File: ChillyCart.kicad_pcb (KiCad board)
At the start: 2 copper layers, 51 x 60.7 mm, 14 parts, among them J1 GameBoy_GamePak_DMG-09, J2 USB_C_Receptacle_USB2.0_16P, U1 TXB0108PW, U2 TXB0108PW, U3 TXB0108PW, U4 RP2350_80QFN

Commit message: Added psram,flash,rtc,sd
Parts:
- added BT1: Battery_Cell, Battery:BatteryHolder_Keystone_103_1x20mm, F.Cu at (150.0, 63.8)
- added C10: 15p, Capacitor_SMD:C_0402_1005Metric, F.Cu at (128.7, 99.0)
- added C11: 100n, Capacitor_SMD:C_0402_1005Metric, F.Cu at (128.7, 101.0)
- added C12: DNF, Capacitor_SMD:C_0402_1005Metric, F.Cu at (166.5, 82.0)
- added C13: 100n, Capacitor_SMD:C_0402_1005Metric, F.Cu at (166.5, 84.0)
- added C14: 100n, Capacitor_SMD:C_0402_1005Metric, F.Cu at (138.1, 94.0)
- added C15: 100n, Capacitor_SMD:C_0402_1005Metric, F.Cu at (131.6, 97.0)
- added C16: 100n, Capacitor_SMD:C_0402_1005Metric, F.Cu at (131.6, 99.0)
- added C17: 100n, Capacitor_SMD:C_0402_1005Metric, F.Cu at (131.6, 101.0)
- added C18: 100n, Capacitor_SMD:C_0402_1005Metric, F.Cu at (169.3, 82.0)
- added C19: 100n, Capacitor_SMD:C_0402_1005Metric, F.Cu at (169.3, 84.0)
- added C20: 100n, Capacitor_SMD:C_0402_1005Metric, F.Cu at (140.9, 94.0)
- added C21: 100n, Capacitor_SMD:C_0402_1005Metric, F.Cu at (134.5, 97.0)
- added C24: 4.7u, Capacitor_SMD:C_0402_1005Metric, F.Cu at (134.5, 99.0)
- added C25: 100n, Capacitor_SMD:C_0402_1005Metric, F.Cu at (134.5, 101.0)
- added C26: 4.7u, Capacitor_SMD:C_0402_1005Metric, F.Cu at (172.2, 82.0)
- added C27: 100n, Capacitor_SMD:C_0402_1005Metric, F.Cu at (172.2, 84.0)
- added C28: 10u, Capacitor_SMD:C_0805_2012Metric, F.Cu at (162.9, 100.5)
- added C7: 10u, Capacitor_SMD:C_0805_2012Metric, F.Cu at (158.9, 100.5)
- added C7: 100nF, Capacitor_SMD:C_0603_1608Metric_Pad1.08x0.95mm_HandSolder, F.Cu at (138.7, 89.2)
- added C8: 100nF, Capacitor_SMD:C_0603_1608Metric_Pad1.08x0.95mm_HandSolder, F.Cu at (138.7, 91.7)
- added C9: 15p, Capacitor_SMD:C_0402_1005Metric, F.Cu at (128.7, 97.0)
- added J3: Micro_SD_Card_Det1, kicad-open-modules:TF-015, F.Cu at (135.5, 83.3)
- added R10: 27, Resistor_SMD:R_0402_1005Metric, F.Cu at (164.2, 82.0)
- added R11: 27, Resistor_SMD:R_0402_1005Metric, F.Cu at (164.2, 84.0)
- added R3: 1k, Resistor_SMD:R_0402_1005Metric, F.Cu at (138.1, 96.0)
- added R4: DNF, Resistor_SMD:R_0402_1005Metric, F.Cu at (158.4, 82.0)
- added R5: 0, Resistor_SMD:R_0402_1005Metric, F.Cu at (158.4, 84.0)
- added R6: DNF, Resistor_SMD:R_0402_1005Metric, F.Cu at (141.0, 96.0)
- added R7: DNF, Resistor_SMD:R_0402_1005Metric, F.Cu at (161.3, 82.0)
- added R8: DNF, Resistor_SMD:R_0402_1005Metric, F.Cu at (161.3, 84.0)
- added R9: 33, Resistor_SMD:R_0402_1005Metric, F.Cu at (143.9, 96.0)
- added U5: AMS1117-3.3, Package_TO_SOT_SMD:SOT-223-3_TabPin2, F.Cu at (131.6, 92.2)
- added U6: W25Q128JVS, Package_SO:SOIC-8_5.23x5.23mm_P1.27mm, F.Cu at (150.5, 96.0)
- added U7: DNF, Package_SO:SOIC-8_5.23x5.23mm_P1.27mm, F.Cu at (150.4, 104.9)
- added U8: MCP7940N-xMNY, Package_DFN_QFN:DFN-8-1EP_3x2mm_P0.5mm_EP1.36x1.46mm, F.Cu at (141.0, 99.8)
- added Y1: ABM8-272-T3, Crystal:Crystal_SMD_3225-4Pin_3.2x2.5mm, F.Cu at (168.0, 100.5)
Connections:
- U4 pad 10: unconnected-(U4-DVDD-Pad10) -> +1V1
- U4 pad 15: unconnected-(U4-IOVDD-Pad15) -> +3V3
- U4 pad 24: unconnected-(U4-IOVDD-Pad24) -> +3V3
- U4 pad 29: unconnected-(U4-IOVDD-Pad29) -> +3V3
- U4 pad 32: unconnected-(U4-DVDD-Pad32) -> +1V1
- U4 pad 41: unconnected-(U4-IOVDD-Pad41) -> +3V3
- U4 pad 5: unconnected-(U4-IOVDD-Pad5) -> +3V3
- U4 pad 50: unconnected-(U4-IOVDD-Pad50) -> +3V3
- U4 pad 51: unconnected-(U4-DVDD-Pad51) -> +1V1
- U4 pad 59: unconnected-(U4-ADC_AVDD-Pad59) -> +3V3
- U4 pad 60: unconnected-(U4-IOVDD-Pad60) -> +3V3
- U4 pad 61: unconnected-(U4-VREG_AVDD-Pad61) -> /VREG_AVDD
- U4 pad 62: unconnected-(U4-VREG_PGND-Pad62) -> GND
- U4 pad 63: unconnected-(U4-VREG_LX-Pad63) -> /VREG_LX
- U4 pad 64: unconnected-(U4-VREG_VIN-Pad64) -> +3V3
- U4 pad 65: unconnected-(U4-VREG_FB-Pad65) -> +1V1
- U4 pad 66: USB_D- -> Net-(U4-USB_DM)
- U4 pad 67: USB_D+ -> Net-(U4-USB_DP)
- U4 pad 68: unconnected-(U4-USB_OTP_VDD-Pad68) -> +3V3
- U4 pad 69: unconnected-(U4-QSPI_IOVDD-Pad69) -> +3V3
- U4 pad 70: unconnected-(U4-QSPI_SD3-Pad70) -> /QSPI_SD3
- U4 pad 71: unconnected-(U4-QSPI_SCLK-Pad71) -> /QSPI_SCLK
- U4 pad 72: unconnected-(U4-QSPI_SD0-Pad72) -> /QSPI_SD0
- U4 pad 73: unconnected-(U4-QSPI_SD2-Pad73) -> /QSPI_SD2
- U4 pad 74: unconnected-(U4-QSPI_SD1-Pad74) -> /QSPI_SD1
- U4 pad 75: unconnected-(U4-QSPI_SS-Pad75) -> /QSPI_SS
- U4 pad 76: unconnected-(U4-IOVDD-Pad76) -> +3V3
- U4 pad 81: unconnected-(U4-GND-Pad81) -> GND

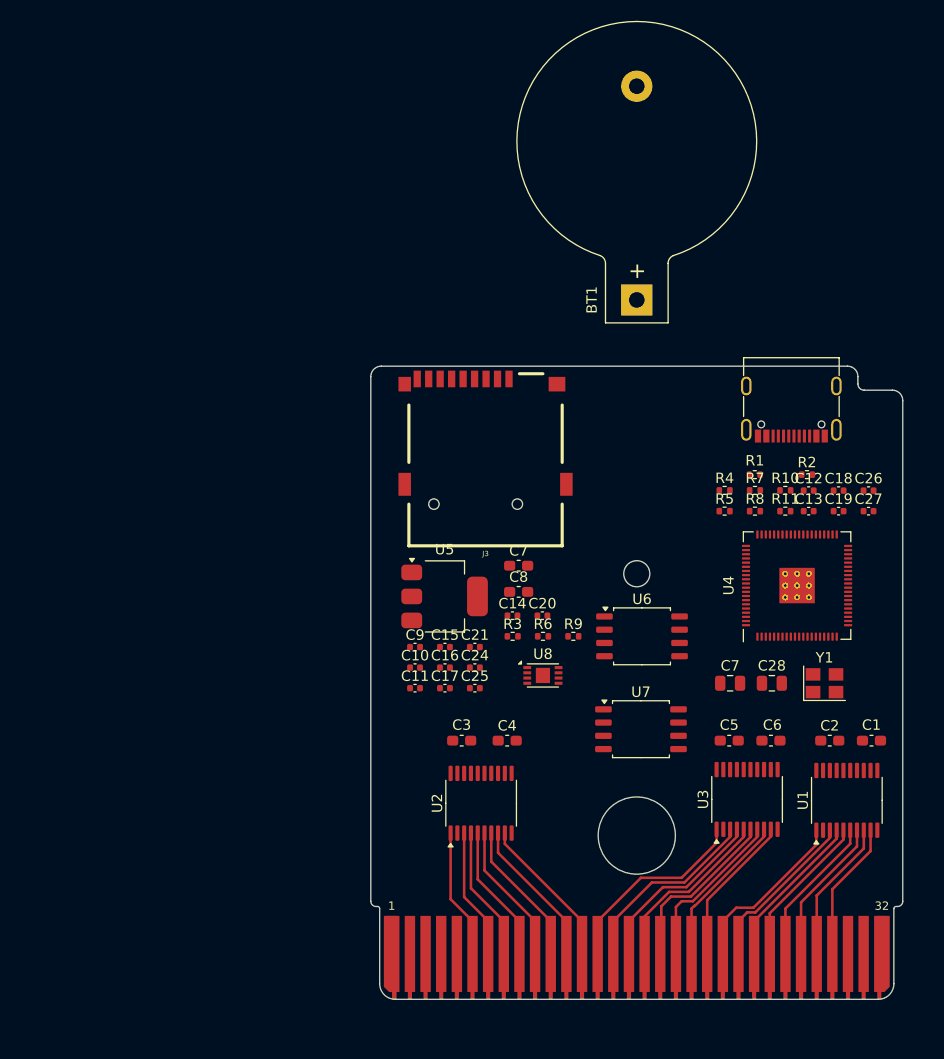
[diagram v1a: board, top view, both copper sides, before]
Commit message: Add IMU, power mux and cleanup schematic
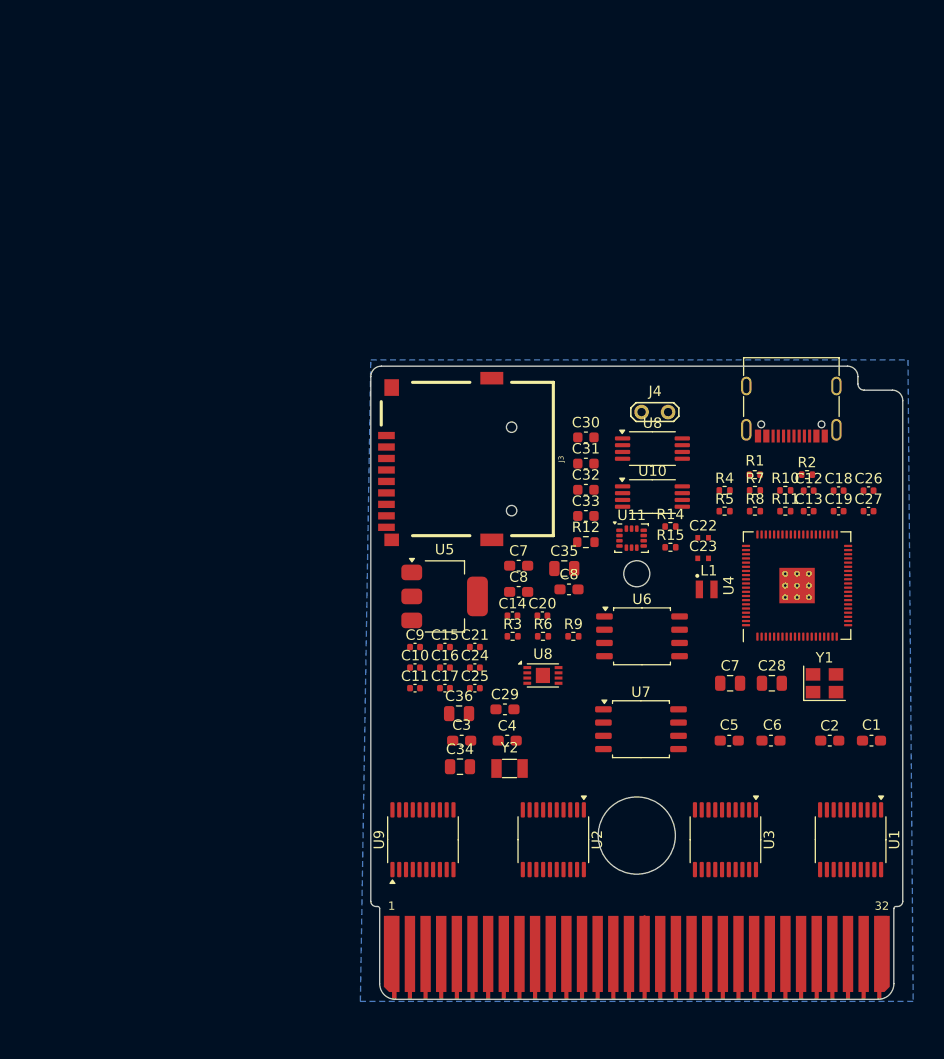
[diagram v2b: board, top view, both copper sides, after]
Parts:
- added C22: 4.7u, RP2350_80QFN_minimal:C_0402_1005Metric_small_pads, F.Cu at (156.4, 86.6)
- added C23: 4.7u, RP2350_80QFN_minimal:C_0402_1005Metric_small_pads, F.Cu at (156.4, 88.5)
- added C29: 100nF, Capacitor_SMD:C_0603_1608Metric_Pad1.08x0.95mm_HandSolder, F.Cu at (137.4, 103.0)
- added C30: 100nF, Capacitor_SMD:C_0603_1608Metric, F.Cu at (145.1, 76.9)
- added C31: 7pF, Capacitor_SMD:C_0603_1608Metric, F.Cu at (145.1, 79.4)
- added C32: 7pF, Capacitor_SMD:C_0603_1608Metric, F.Cu at (145.1, 82.0)
- added C33: 100nF, Capacitor_SMD:C_0603_1608Metric, F.Cu at (145.1, 84.5)
- added C34: 47uF, Capacitor_SMD:C_0805_2012Metric, F.Cu at (133.1, 108.5)
- added C35: 10u, Capacitor_SMD:C_0805_2012Metric, F.Cu at (143.1, 89.5)
- added C36: 100n, Capacitor_SMD:C_0805_2012Metric, F.Cu at (133.0, 103.4)
- added C8: 100nF, Capacitor_SMD:C_0603_1608Metric_Pad1.08x0.95mm_HandSolder, F.Cu at (143.5, 91.5)
- added J4: Conn_01x02_Socket, TestPoint:TestPoint_2Pads_Pitch2.54mm_Drill0.8mm, F.Cu at (150.5, 74.5)
- added L1: 3.3u, RP2350_80QFN_minimal:L_pol_2016, F.Cu at (156.7, 91.5)
- added R12: 10k, Resistor_SMD:R_0603_1608Metric, F.Cu at (145.1, 87.0)
- added R14: 1k, Resistor_SMD:R_0402_1005Metric, F.Cu at (153.2, 85.5)
- added R15: 1k, Resistor_SMD:R_0402_1005Metric, F.Cu at (153.2, 87.5)
- added U10: MCP7940N-x/ST, Package_SO:TSSOP-8_4.4x3mm_P0.65mm, F.Cu at (151.5, 82.6)
- added U11: LSM6DS3, Package_LGA:LGA-14_3x2.5mm_P0.5mm_LayoutBorder3x4y, F.Cu at (149.5, 86.6)
- added U8: TPS2111A, Package_SO:TSSOP-8_4.4x3mm_P0.65mm, F.Cu at (151.5, 78.0)
- added U9: TXB0108PW, Package_SO:TSSOP-20_4.4x6.5mm_P0.65mm, F.Cu at (129.5, 115.5)
- added Y2: FC-135, Crystal:Crystal_SMD_3215-2Pin_3.2x1.5mm, F.Cu at (137.8, 108.7)
- BT1: footprint Battery:BatteryHolder_Keystone_103_1x20mm -> Battery:Battery_CR1225
- moved BT1 35.1 mm to (183.7, 73.4), turned to 0 degrees
- moved U2 7.76 mm to (142.0, 115.5), turned to -90 degrees
- moved J3 5.00 mm to (138.0, 79.0), turned to 90 degrees
- moved U3 4.38 mm to (158.5, 115.5), turned to -90 degrees
- moved U1 3.79 mm to (170.5, 115.5), turned to -90 degrees
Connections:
- C2 pad 2: VCC -> +5V_CART
- C28 pad 1: VCC -> Net-(U5-VI)
- C4 pad 2: VCC -> +5V_CART
- C6 pad 2: VCC -> +5V_CART
- C9 pad 1: /XIN -> Net-(U4-XIN)
- J1 pad 1: VCC -> +5V_CART
- J1 pad 2: unconnected-(J1-PHI-Pad2) -> CLK
- J1 pad 3: unconnected-(J1-~{WR}-Pad3) -> WR
- J1 pad 30: unconnected-(J1-~{RST}-Pad30) -> RST
- J1 pad 4: unconnected-(J1-~{RD}-Pad4) -> RD
- J1 pad 5: unconnected-(J1-~{CS}-Pad5) -> CS
- J3 pad 10: unconnected-(J3-SHIELD-Pad10) -> GND
- J3 pad 2: unconnected-(J3-DAT3/CD-Pad2) -> SD_DAT3
- J3 pad 3: unconnected-(J3-CMD-Pad3) -> SD_MOSI
- J3 pad 4: unconnected-(J3-VDD-Pad4) -> +3V3
- J3 pad 5: unconnected-(J3-CLK-Pad5) -> SD_CLK
- J3 pad 6: unconnected-(J3-VSS-Pad6) -> GND
- J3 pad 7: unconnected-(J3-DAT0-Pad7) -> SD_MISO
- J3 pad 9: unconnected-(J3-DET-Pad9) -> SD_DET
- R3 pad 1: /XOUT -> Net-(U4-XOUT)
- U1 pad 1: DATA0 -> RP_DATA7
- U1 pad 10: POWER_GOOD -> unconnected-(U1-OE-Pad10)
- U1 pad 12: RP_DATA7 -> DATA0
- U1 pad 13: RP_DATA6 -> DATA1
- U1 pad 14: RP_DATA5 -> DATA2
- U1 pad 15: RP_DATA4 -> DATA3
- U1 pad 16: RP_DATA3 -> DATA4
- U1 pad 17: RP_DATA2 -> DATA5
- U1 pad 18: RP_DATA1 -> DATA6
- U1 pad 19: VCC -> +5V_CART
- U1 pad 20: RP_DATA0 -> DATA7
- U1 pad 3: DATA1 -> RP_DATA6
- U1 pad 4: DATA2 -> RP_DATA5
- U1 pad 5: DATA3 -> RP_DATA4
- U1 pad 6: DATA4 -> RP_DATA3
- U1 pad 7: DATA5 -> RP_DATA2
- U1 pad 8: DATA6 -> RP_DATA1
- U1 pad 9: DATA7 -> RP_DATA0
- U2 pad 1: ADDR0 -> RP_ADDR7
- U2 pad 10: POWER_GOOD -> unconnected-(U2-OE-Pad10)
- U2 pad 12: RP_ADDR7 -> ADDR0
- U2 pad 13: RP_ADDR6 -> ADDR1
- U2 pad 14: RP_ADDR5 -> ADDR2
- U2 pad 15: RP_ADDR4 -> ADDR3
- U2 pad 16: RP_ADDR3 -> ADDR4
- U2 pad 17: RP_ADDR2 -> ADDR5
- U2 pad 18: RP_ADDR1 -> ADDR6
- U2 pad 19: VCC -> +5V_CART
- U2 pad 20: RP_ADDR0 -> ADDR7
- U2 pad 3: ADDR1 -> RP_ADDR6
- U2 pad 4: ADDR2 -> RP_ADDR5
- U2 pad 5: ADDR3 -> RP_ADDR4
- U2 pad 6: ADDR4 -> RP_ADDR3
- U2 pad 7: ADDR5 -> RP_ADDR2
- U2 pad 8: ADDR6 -> RP_ADDR1
- U2 pad 9: ADDR7 -> RP_ADDR0
- U3 pad 1: ADDR8 -> RP_ADDR15
- U3 pad 10: POWER_GOOD -> unconnected-(U3-OE-Pad10)
- U3 pad 12: RP_ADDR15 -> ADDR8
- U3 pad 13: RP_ADDR14 -> ADDR9
- U3 pad 14: RP_ADDR13 -> ADDR10
- U3 pad 15: RP_ADDR12 -> ADDR11
- U3 pad 16: RP_ADDR11 -> ADDR12
- U3 pad 17: RP_ADDR10 -> ADDR13
- U3 pad 18: RP_ADDR9 -> ADDR14
- U3 pad 19: VCC -> +5V_CART
- U3 pad 20: RP_ADDR8 -> ADDR15
- U3 pad 3: ADDR9 -> RP_ADDR14
- U3 pad 4: ADDR10 -> RP_ADDR13
- U3 pad 5: ADDR11 -> RP_ADDR12
- U3 pad 6: ADDR12 -> RP_ADDR11
- U3 pad 7: ADDR13 -> RP_ADDR10
- U3 pad 8: ADDR14 -> RP_ADDR9
- U3 pad 9: ADDR15 -> RP_ADDR8
- U4 pad 1: RP_ADDR4 -> RP_ADDR3
- U4 pad 11: RP_ADDR12 -> RP_ADDR11
- U4 pad 12: RP_ADDR13 -> RP_ADDR12
- U4 pad 13: RP_ADDR14 -> RP_ADDR13
- U4 pad 14: RP_ADDR15 -> RP_ADDR14
- U4 pad 16: RP_DATA0 -> RP_ADDR15
- U4 pad 17: RP_DATA1 -> RP_DATA0
- U4 pad 18: RP_DATA2 -> RP_DATA1
- U4 pad 19: RP_DATA3 -> RP_DATA2
- U4 pad 2: RP_ADDR5 -> RP_ADDR4
- U4 pad 20: RP_DATA4 -> RP_DATA3
- U4 pad 21: RP_DATA5 -> RP_DATA4
- U4 pad 22: RP_DATA6 -> RP_DATA5
- U4 pad 23: RP_DATA7 -> RP_DATA6
- U4 pad 25: unconnected-(U4-GPIO24-Pad25) -> RP_DATA7
- U4 pad 26: unconnected-(U4-GPIO25-Pad26) -> RP_CLK
- U4 pad 27: unconnected-(U4-GPIO26-Pad27) -> RP_WR
- U4 pad 28: unconnected-(U4-GPIO27-Pad28) -> RP_RD
- U4 pad 3: RP_ADDR6 -> RP_ADDR5
- U4 pad 30: unconnected-(U4-XIN-Pad30) -> Net-(U4-XIN)
- U4 pad 31: unconnected-(U4-XOUT-Pad31) -> Net-(U4-XOUT)
- U4 pad 36: unconnected-(U4-GPIO28-Pad36) -> RP_CS
- U4 pad 37: unconnected-(U4-GPIO29-Pad37) -> RP_RST
- U4 pad 38: unconnected-(U4-GPIO30-Pad38) -> RTC_SDA
- U4 pad 39: unconnected-(U4-GPIO31-Pad39) -> RTC_SCL
- U4 pad 4: RP_ADDR7 -> RP_ADDR6
- U4 pad 40: unconnected-(U4-GPIO32-Pad40) -> SD_MISO
- U4 pad 42: unconnected-(U4-GPIO33-Pad42) -> SD_DAT3
- U4 pad 43: unconnected-(U4-GPIO34-Pad43) -> SD_CLK
- U4 pad 44: unconnected-(U4-GPIO35-Pad44) -> SD_MOSI
- U4 pad 45: unconnected-(U4-GPIO36-Pad45) -> IMU_SDA
- U4 pad 46: unconnected-(U4-GPIO37-Pad46) -> IMU_SCL
- U4 pad 47: unconnected-(U4-GPIO38-Pad47) -> SD_DET
- U4 pad 48: unconnected-(U4-GPIO39-Pad48) -> RP_POWER
- U4 pad 6: RP_ADDR8 -> RP_ADDR7
- U4 pad 7: RP_ADDR9 -> RP_ADDR8
- U4 pad 77: RP_ADDR0 -> /GPIO0
- U4 pad 78: RP_ADDR1 -> RP_ADDR0
- U4 pad 79: RP_ADDR2 -> RP_ADDR1
- U4 pad 8: RP_ADDR10 -> RP_ADDR9
- U4 pad 80: RP_ADDR3 -> RP_ADDR2
- U4 pad 9: RP_ADDR11 -> RP_ADDR10
- U5 pad 3: VCC -> Net-(U5-VI)
- Y1 pad 1: /XIN -> Net-(U4-XIN)
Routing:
- net ADDR8: track 15.8 -> 0.00 mm
- net ADDR9: track 15.3 -> 0.00 mm
- net ADDR10: track 15.1 -> 0.00 mm
- net DATA0: track 13.4 -> 0.00 mm
- net ADDR11: track 13.8 -> 0.45 mm
- net ADDR12: track 13.5 -> 0.14 mm
- net DATA1: track 12.8 -> 0.00 mm
- net ADDR13: track 12.7 -> 0.00 mm
- net DATA2: track 12.0 -> 0.00 mm
- net ADDR14: track 11.7 -> 0.00 mm
- net DATA3: track 11.6 -> 0.00 mm
- net ADDR7: track 11.5 -> 0.00 mm
- net ADDR15: track 11.3 -> 0.00 mm
- net DATA4: track 11.3 -> 0.00 mm
- net ADDR6: track 11.2 -> 0.00 mm
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- added copper zone on B.Cu, net GND

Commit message: Initial routing
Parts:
- removed BT1: Battery_Cell, Battery:Battery_CR1225
- removed the C8 at (138.7, 91.7)
- removed the U8 at (141.0, 99.8)
- added J5: Conn_01x02_Socket, TestPoint:TestPoint_2Pads_Pitch2.54mm_Drill0.8mm, F.Cu at (113.2, 77.5)
- added R13: 470R, Resistor_SMD:R_0402_1005Metric_Pad0.72x0.64mm_HandSolder, F.Cu at (97.9, 65.3)
- added SW1: SW_Push, Button_Switch_SMD:SW_Push_1P1T_XKB_TS-1187A, F.Cu at (150.0, 85.4)
- C1, C2, C29, C3, C4, C5, C6, C8: footprint Capacitor_SMD:C_0603_1608Metric_Pad1.08x0.95mm_HandSolder -> Capacitor_SMD:C_0402_1005Metric_Pad0.74x0.62mm_HandSolder
- C10, C11, C12, C13, C14, C15, C16, C17, C18, C19, C20, C21, C24, C25, C26, C27, C9: footprint Capacitor_SMD:C_0402_1005Metric -> Capacitor_SMD:C_0402_1005Metric_Pad0.74x0.62mm_HandSolder
- C22, C23: footprint RP2350_80QFN_minimal:C_0402_1005Metric_small_pads -> Capacitor_SMD:C_0402_1005Metric_Pad0.74x0.62mm_HandSolder
- C28, C34, C35, C36, C7: footprint Capacitor_SMD:C_0805_2012Metric -> Capacitor_SMD:C_0402_1005Metric_Pad0.74x0.62mm_HandSolder
- C30, C31, C32, C33: footprint Capacitor_SMD:C_0603_1608Metric -> Capacitor_SMD:C_0402_1005Metric_Pad0.74x0.62mm_HandSolder
- R1, R10, R11, R14, R15, R2, R3, R4, R5, R6, R7, R8, R9: footprint Resistor_SMD:R_0402_1005Metric -> Resistor_SMD:R_0402_1005Metric_Pad0.72x0.64mm_HandSolder
- R12: footprint Resistor_SMD:R_0603_1608Metric -> Resistor_SMD:R_0402_1005Metric_Pad0.72x0.64mm_HandSolder
- moved C28 76.8 mm to (96.8, 61.5)
- moved C7 76.8 mm to (92.8, 61.5)
- moved U8 56.4 mm to (95.5, 71.5)
- moved R14 53.7 mm to (103.2, 66.0)
- moved R15 53.7 mm to (103.2, 68.0)
- moved C10 44.4 mm to (173.0, 103.0)
- moved C12 39.6 mm to (133.9, 104.5)
- moved C9 39.2 mm to (167.4, 103.5)
- moved C35 38.5 mm to (107.6, 74.3)
- moved C7 38.5 mm to (103.3, 74.1)
- moved U5 38.5 mm to (95.1, 80.0)
- moved C36 37.9 mm to (169.0, 91.8), turned to 90 degrees
- moved Y2 36.6 mm to (173.2, 99.8), turned to 180 degrees
- moved C15 36.0 mm to (167.4, 101.0)
- moved C16 35.9 mm to (167.4, 97.5)
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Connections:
- net Net-(J4-Pin_1) renamed /+VBAT
- U1 pad 10: unconnected-(U1-OE-Pad10) -> +3V3
- U2 pad 10: unconnected-(U2-OE-Pad10) -> +3V3
- U3 pad 10: unconnected-(U3-OE-Pad10) -> +3V3
- U4 pad 26: RP_CLK -> RP_RST
- U4 pad 27: RP_WR -> RP_CS
- U4 pad 33: unconnected-(U4-SWCLK-Pad33) -> Net-(J5-Pin_2)
- U4 pad 34: unconnected-(U4-SWD-Pad34) -> Net-(J5-Pin_1)
- U4 pad 35: unconnected-(U4-RUN-Pad35) -> +3V3
- U4 pad 36: RP_CS -> RP_WR
- U4 pad 37: RP_RST -> RP_CLK
- U4 pad 49: unconnected-(U4-GPIO40_ADC0-Pad49) -> Net-(U4-GPIO40_ADC0)
- U4 pad 52: unconnected-(U4-GPIO41_ADC1-Pad52) -> Net-(J7-Pin_1)
- U4 pad 53: unconnected-(U4-GPIO42_ADC2-Pad53) -> Net-(J7-Pin_2)
- U4 pad 54: unconnected-(U4-GPIO43_ADC3-Pad54) -> Net-(J7-Pin_3)
- U4 pad 55: unconnected-(U4-GPIO44_ADC4-Pad55) -> Net-(J7-Pin_4)
- U4 pad 56: unconnected-(U4-GPIO45_ADC5-Pad56) -> Net-(J7-Pin_5)
- U4 pad 57: unconnected-(U4-GPIO46_ADC6-Pad57) -> Net-(J7-Pin_6)
- U4 pad 58: unconnected-(U4-GPIO47_ADC7-Pad58) -> Net-(J7-Pin_7)
- U9 pad 1: CLK -> unconnected-(U9-A1-Pad1)
- U9 pad 10: unconnected-(U9-OE-Pad10) -> +3V3
- U9 pad 12: unconnected-(U9-B8-Pad12) -> CLK
- U9 pad 13: unconnected-(U9-B7-Pad13) -> WR
- U9 pad 14: RP_POWER -> RD
- U9 pad 15: RP_RST -> CS
- U9 pad 16: RP_CS -> RST
- U9 pad 17: RP_RD -> +5V_CART
- U9 pad 18: RP_WR -> unconnected-(U9-B2-Pad18)
- U9 pad 20: RP_CLK -> unconnected-(U9-B1-Pad20)
- U9 pad 3: WR -> unconnected-(U9-A2-Pad3)
- U9 pad 4: RD -> RP_POWER
- U9 pad 5: CS -> RP_RST
- U9 pad 6: RST -> RP_CS
- U9 pad 7: +5V_CART -> RP_RD
- U9 pad 8: unconnected-(U9-A7-Pad8) -> RP_WR
- U9 pad 9: unconnected-(U9-A8-Pad9) -> RP_CLK
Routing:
- net +3V3: track 0.00 -> 84.7 mm
- net RST: track 0.00 -> 59.4 mm, vias 0 -> 2
- net RP_RD: track 0.00 -> 45.1 mm, vias 0 -> 2
- net RP_CS: track 0.00 -> 44.7 mm, vias 0 -> 2
- net RP_POWER: track 0.00 -> 43.1 mm, vias 0 -> 2
- net RP_RST: track 0.00 -> 42.2 mm, vias 0 -> 2
- net /QSPI_SD2: track 0.00 -> 40.6 mm
- net /QSPI_SD1: track 0.00 -> 37.0 mm, vias 0 -> 2
- net +5V_CART: track 0.00 -> 37.0 mm
- net USB_D-: track 0.00 -> 30.7 mm
- net USB_D+: track 0.00 -> 29.8 mm
- net /GPIO0: track 0.00 -> 27.7 mm, vias 0 -> 2
- net /QSPI_SD3: track 0.00 -> 24.1 mm, vias 0 -> 2
- net Net-(U4-GPIO40_ADC0): track 0.00 -> 23.6 mm
- net /QSPI_SCLK: track 0.00 -> 22.4 mm, vias 0 -> 2
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- removed copper zone on B.Cu, net GND

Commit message: Finish routingn
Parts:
- removed the C7 at (103.3, 74.1)
- added J6: Conn_01x02_Socket, TestPoint:TestPoint_2Pads_Pitch2.54mm_Drill0.8mm, F.Cu at (140.0, 92.0)
- added J7: Conn_01x09_Socket, Connector_PinHeader_1.00mm:PinHeader_1x09_P1.00mm_Vertical, F.Cu at (157.5, 71.5)
- added R16: 1k, Resistor_SMD:R_0402_1005Metric_Pad0.72x0.64mm_HandSolder, F.Cu at (136.9, 92.5)
- moved C28 48.0 mm to (137.0, 87.8), turned to -90 degrees
- moved J5 47.9 mm to (160.8, 71.5)
- moved C7 47.7 mm to (139.2, 72.5)
- moved U5 45.4 mm to (140.5, 78.3), turned to 90 degrees
- moved R13 39.6 mm to (128.4, 90.5)
- moved U8 39.4 mm to (131.5, 87.5)
- moved R14 32.7 mm to (130.5, 84.0), turned to 180 degrees
- moved R15 29.1 mm to (127.5, 84.0), turned to 180 degrees
- moved C35 27.6 mm to (133.5, 84.0)
- moved C27 16.3 mm to (164.0, 96.5), turned to 90 degrees
- moved J4 5.74 mm to (143.0, 71.5)
- moved C26 1.75 mm to (150.4, 103.5)
- moved C18 1.05 mm to (149.0, 106.5)
- moved Y2 0.75 mm to (172.5, 99.8)
- moved C21 0.73 mm to (149.1, 101.1)
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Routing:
- net +3V3: track 84.7 -> 317.1 mm, vias 0 -> 26
- net GND: track 0.00 -> 138.1 mm, vias 0 -> 63
- net +5V_CART: track 37.0 -> 100.9 mm, vias 0 -> 2
- net RP_CLK: track 0.00 -> 57.8 mm, vias 0 -> 2
- net RP_WR: track 0.00 -> 55.6 mm, vias 0 -> 2
- net /+VBAT: track 0.00 -> 52.1 mm
- net Net-(J5-Pin_2): track 0.00 -> 45.8 mm, vias 0 -> 2
- net Net-(J7-Pin_1): track 0.00 -> 41.2 mm, vias 0 -> 4
- net +1V1: track 4.15 -> 44.6 mm, vias 0 -> 7
- net Net-(J7-Pin_4): track 0.00 -> 39.3 mm, vias 0 -> 4
- net /QSPI_SS: track 0.00 -> 38.6 mm, vias 0 -> 2
- net Net-(J7-Pin_5): track 0.00 -> 37.7 mm, vias 0 -> 2
- net Net-(J5-Pin_1): track 0.00 -> 37.1 mm, vias 0 -> 4
- net Net-(J7-Pin_6): track 0.00 -> 37.0 mm, vias 0 -> 2
- net Net-(J7-Pin_7): track 0.00 -> 36.3 mm, vias 0 -> 2
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- added copper zone on F.Cu, net +1V1
- added copper zone on F.Cu, net +3V3
- added copper zone on B.Cu, net GND
